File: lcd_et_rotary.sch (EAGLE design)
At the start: 7 parts, among them IC1 74LS595N, SW1 ROTARTY_ENCODER, U1 LCD-16X2SILK

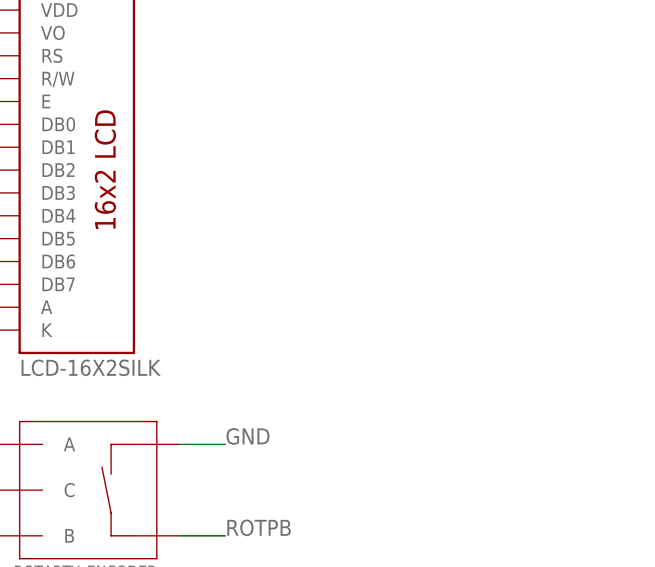
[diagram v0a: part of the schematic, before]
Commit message: added a note about current limiting on the backlight
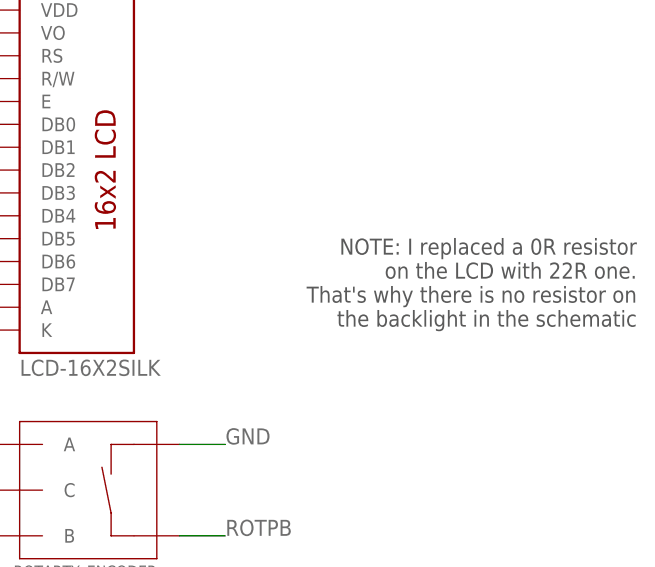
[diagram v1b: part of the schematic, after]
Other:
- note added: "NOTE: I replaced a 0R resistor on the LCD with 22R one. That's why there is no resistor on the backlight in the schematic"
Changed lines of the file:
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@@
 <sheet>
 <plain>
+<text x="157.48" y="40.64" size="1.778" layer="97" rot="R180">NOTE: I replaced a 0R resistor
+on the LCD with 22R one.
+That's why there is no resistor on
+the backlight in the schematic</text>
 </plain>
 <instances>
@@
 </schematic>
 </drawing>
+<compatibility>
+<note version="6.3" minversion="6.2.2" severity="warning">
+Since Version 6.2.2 text objects can contain more than one line,
+which will not be processed correctly with this version.
+</note>
+</compatibility>
 </eagle>

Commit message: reminder
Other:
- note added: "Arduino pins: MOSI = A0 CLK = A1 SS = A2"
- note added: "Arduino pins: ROTA = A3 ROTB = A4 ROTPB = A5"
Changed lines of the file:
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@@
 That's why there is no resistor on
 the backlight in the schematic</text>
+<text x="-10.16" y="66.04" size="1.778" layer="97">Arduino pins:
+MOSI = A0
+CLK = A1
+SS = A2</text>
+<text x="-12.7" y="12.7" size="1.778" layer="97">Arduino pins:
+ROTA = A3
+ROTB = A4
+ROTPB = A5</text>
 </plain>
 <instances>

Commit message: the way it was actually built on veroboard
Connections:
- net N$4 renamed DB5
- removed net N$1: IC1.QH, U1.A
- removed net N$2: IC1.QG, U1.DB7
- removed net N$3: IC1.QF, U1.DB6
- removed net N$5: IC1.QD, U1.DB4
- removed net N$6: IC1.QA, U1.E
- removed net N$7: IC1.QB, U1.R/W
- removed net N$8: IC1.QC, U1.RS
- new net BL+: IC1.QB, U1.A
- new net DB4: IC1.QF, U1.DB4
- new net DB6: IC1.QD, U1.DB6
- new net DB7: IC1.QC, U1.DB7
- new net E: IC1.QG, U1.E
- new net RS: IC1.QA, U1.RS
- new net RW: IC1.QH, U1.R/W
- net CLK: now also LCD_CTRL.1; no longer LCD_CTRL.2
- net SS: now also LCD_CTRL.2; no longer LCD_CTRL.1
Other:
- note added: "Arduino pins: MOSI = A0 SS = A1 CLK = A2"
- note removed: "Arduino pins: MOSI = A0 CLK = A1 SS = A2"
- moved on the sheet: SW1, U1

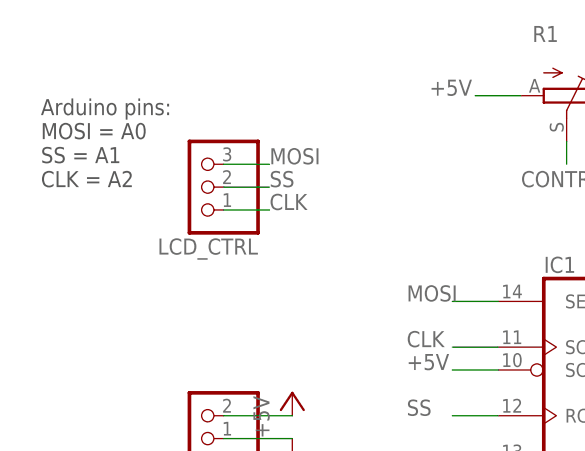
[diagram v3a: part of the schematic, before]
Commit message: keep schematic and sketch consistent
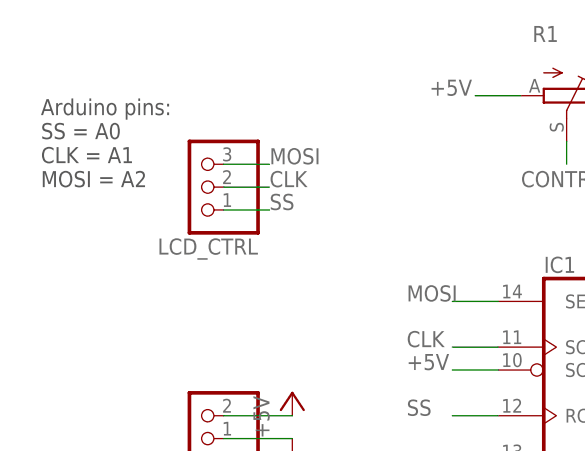
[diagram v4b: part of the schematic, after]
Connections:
- net CLK: now also LCD_CTRL.2; no longer LCD_CTRL.1
- net SS: now also LCD_CTRL.1; no longer LCD_CTRL.2
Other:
- note added: "Arduino pins: SS = A0 CLK = A1 MOSI = A2"
- note removed: "Arduino pins: MOSI = A0 SS = A1 CLK = A2"
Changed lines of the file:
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@@
 the backlight in the schematic</text>
 <text x="-10.16" y="66.04" size="1.778" layer="97">Arduino pins:
-MOSI = A0
-SS = A1
-CLK = A2</text>
+SS = A0
+CLK = A1
+MOSI = A2</text>
 <text x="-12.7" y="12.7" size="1.778" layer="97">Arduino pins:
 ROTA = A3
@@
 </segment>
 <segment>
-<pinref part="LCD_CTRL" gate="A" pin="1"/>
-<wire x1="10.16" y1="63.5" x2="15.24" y2="63.5" width="0.1524" layer="91"/>
-<label x="15.24" y="63.5" size="1.778" layer="95"/>
+<pinref part="LCD_CTRL" gate="A" pin="2"/>
+<wire x1="10.16" y1="66.04" x2="15.24" y2="66.04" width="0.1524" layer="91"/>
+<label x="15.24" y="66.04" size="1.778" layer="95"/>
 </segment>
 </net>
@@
 </segment>
 <segment>
-<pinref part="LCD_CTRL" gate="A" pin="2"/>
-<wire x1="10.16" y1="66.04" x2="15.24" y2="66.04" width="0.1524" layer="91"/>
-<label x="15.24" y="66.04" size="1.778" layer="95"/>
+<pinref part="LCD_CTRL" gate="A" pin="1"/>
+<wire x1="10.16" y1="63.5" x2="15.24" y2="63.5" width="0.1524" layer="91"/>
+<label x="15.24" y="63.5" size="1.778" layer="95"/>
 </segment>
 </net>

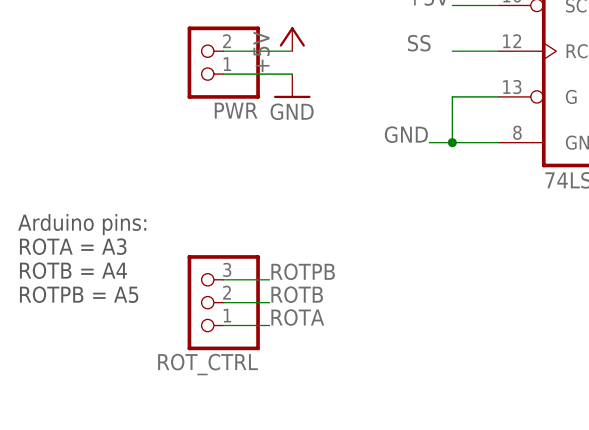
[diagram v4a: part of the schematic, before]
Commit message: some more pins swapped
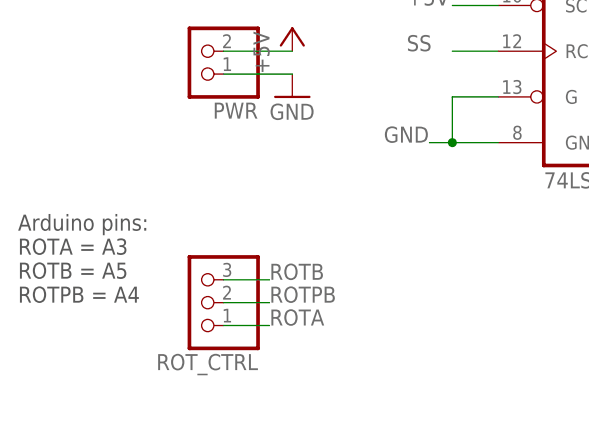
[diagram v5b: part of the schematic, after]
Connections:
- net ROTB: now also ROT_CTRL.3; no longer ROT_CTRL.2
- net ROTPB: now also ROT_CTRL.2; no longer ROT_CTRL.3
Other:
- note added: "Arduino pins: ROTA = A3 ROTB = A5 ROTPB = A4"
- note removed: "Arduino pins: ROTA = A3 ROTB = A4 ROTPB = A5"
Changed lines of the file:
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@@
 <text x="-12.7" y="12.7" size="1.778" layer="97">Arduino pins:
 ROTA = A3
-ROTB = A4
-ROTPB = A5</text>
+ROTB = A5
+ROTPB = A4</text>
 </plain>
 <instances>
@@
 </segment>
 <segment>
-<pinref part="ROT_CTRL" gate="A" pin="3"/>
-<wire x1="10.16" y1="15.24" x2="15.24" y2="15.24" width="0.1524" layer="91"/>
-<label x="15.24" y="15.24" size="1.778" layer="95"/>
+<pinref part="ROT_CTRL" gate="A" pin="2"/>
+<wire x1="10.16" y1="12.7" x2="15.24" y2="12.7" width="0.1524" layer="91"/>
+<label x="15.24" y="12.7" size="1.778" layer="95"/>
 </segment>
 </net>
@@
 </segment>
 <segment>
-<pinref part="ROT_CTRL" gate="A" pin="2"/>
-<wire x1="10.16" y1="12.7" x2="15.24" y2="12.7" width="0.1524" layer="91"/>
-<label x="15.24" y="12.7" size="1.778" layer="95"/>
+<pinref part="ROT_CTRL" gate="A" pin="3"/>
+<wire x1="10.16" y1="15.24" x2="15.24" y2="15.24" width="0.1524" layer="91"/>
+<label x="15.24" y="15.24" size="1.778" layer="95"/>
 </segment>
 </net>

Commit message: some notes
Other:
- note added: "There's a 2.2uF cap on the power input not drawn here, no separate bypass cap for the 595 (you should add one)"
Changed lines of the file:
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@@
 ROTB = A5
 ROTPB = A4</text>
+<text x="25.4" y="12.7" size="1.778" layer="97">There's a 2.2uF cap on the power input
+not drawn here, no separate bypass cap
+for the 595 (you should add one)</text>
 </plain>
 <instances>
